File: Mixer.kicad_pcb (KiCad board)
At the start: 2 copper layers, 59.9 x 100 mm, 48 parts, among them J1 AudioJack2_Ground_Switch, J2 AudioJack2_Ground_Switch, J3 AudioJack2_Ground_Switch, J4 AudioJack2_Ground_Switch, J5 AudioJack2_Ground_Switch, J6 AudioJack2_Ground_Switch, J7 Conn_02x05_Odd_Even, U1 TL074

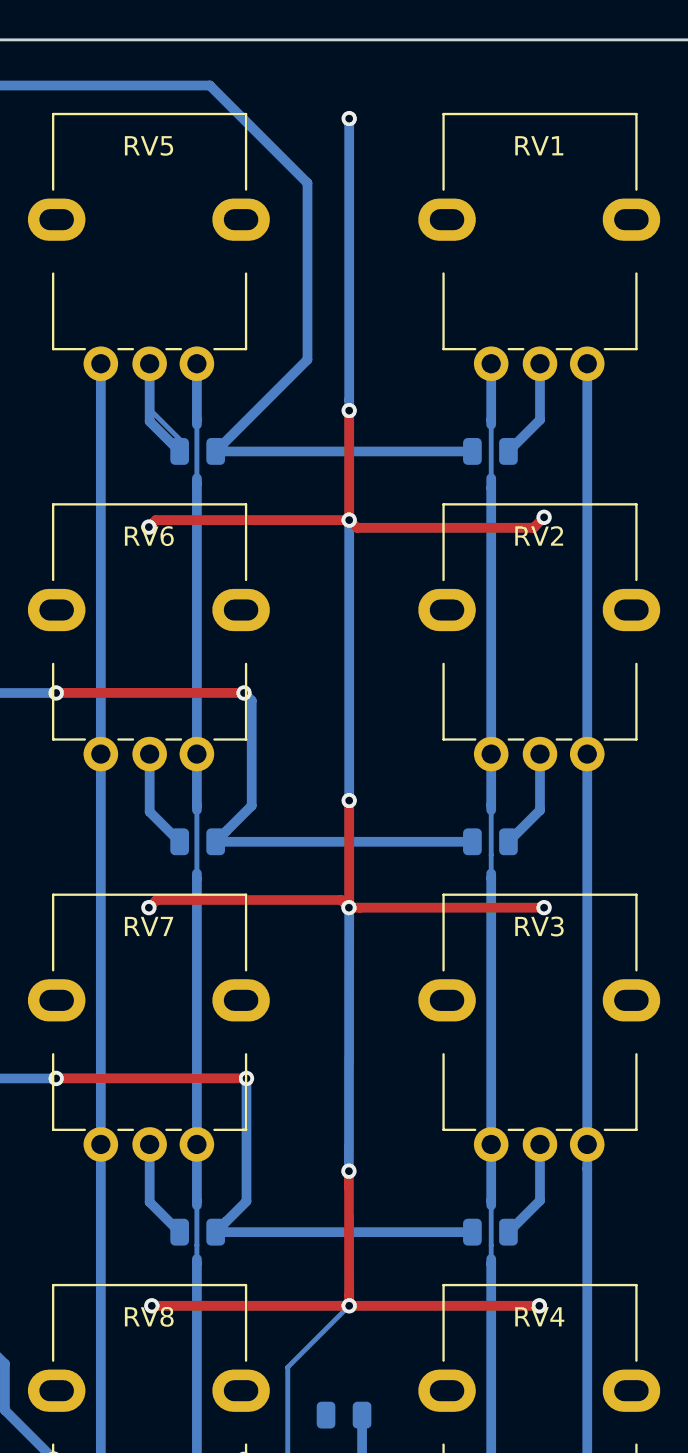
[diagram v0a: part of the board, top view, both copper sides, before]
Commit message: Updated silk-screen with voltages.
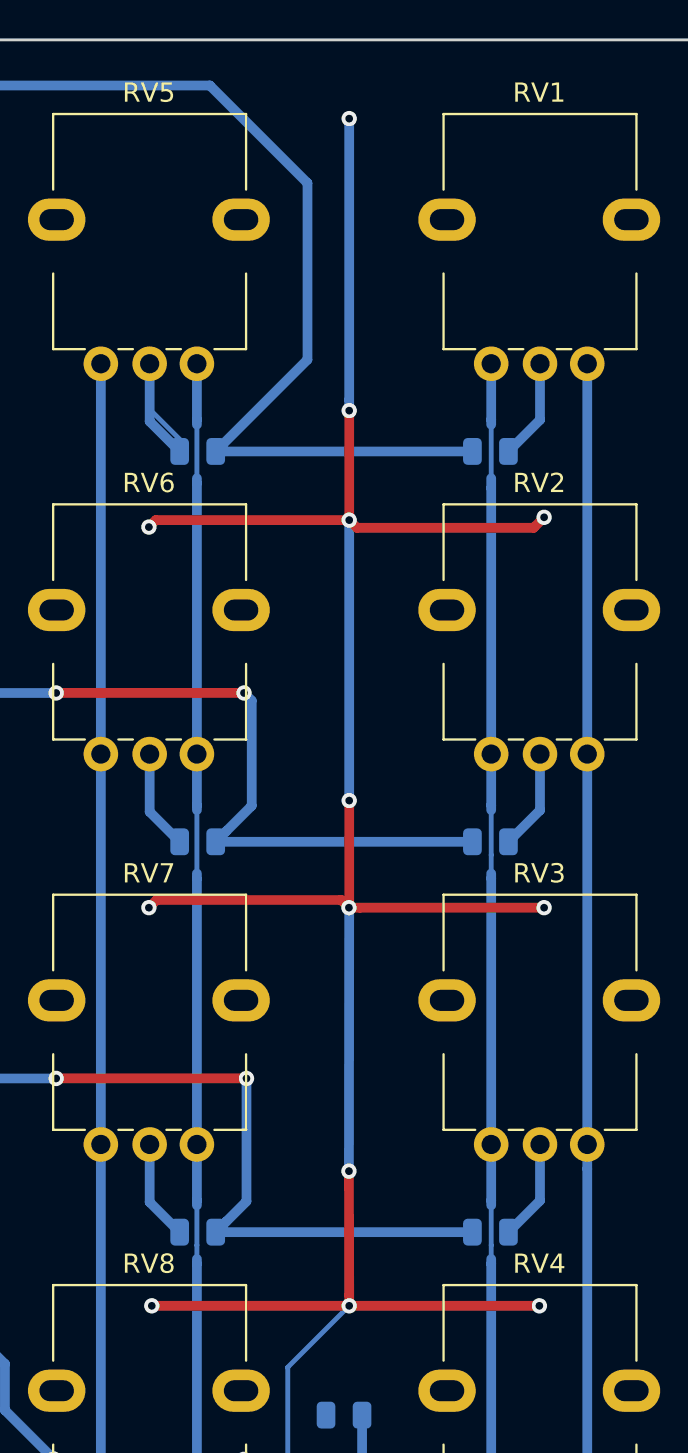
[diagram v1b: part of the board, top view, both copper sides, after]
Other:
- board text added: "+12"
- board text added: "-12"
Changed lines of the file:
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@@
   (general
     (thickness 1.6)
-    (drawings 61)
+    (drawings 64)
     (tracks 329)
     (zones 0)
@@
     (descr "Potentiometer, vertical, Alps RK09K Single, http://www.alps.com/prod/info/E/HTML/Potentiometer/RotaryPotentiometers/RK09K/RK09K_list.html")
     (tags "Potentiometer vertical Alps RK09K Single")
-    (fp_text reference RV8 (at 0 -3.81 180) (layer F.SilkS)
+    (fp_text reference RV8 (at 0 -6.604 180) (layer F.SilkS)
       (effects (font (size 1 1) (thickness 0.15)))
     )
@@
     (descr "Potentiometer, vertical, Alps RK09K Single, http://www.alps.com/prod/info/E/HTML/Potentiometer/RotaryPotentiometers/RK09K/RK09K_list.html")
     (tags "Potentiometer vertical Alps RK09K Single")
-    (fp_text reference RV7 (at 0 -3.81 180) (layer F.SilkS)
+    (fp_text reference RV7 (at 0 -6.604 180) (layer F.SilkS)
       (effects (font (size 1 1) (thickness 0.15)))
     )
@@
     (descr "Potentiometer, vertical, Alps RK09K Single, http://www.alps.com/prod/info/E/HTML/Potentiometer/RotaryPotentiometers/RK09K/RK09K_list.html")
     (tags "Potentiometer vertical Alps RK09K Single")
-    (fp_text reference RV6 (at 0 -3.81 180) (layer F.SilkS)
+    (fp_text reference RV6 (at 0 -6.604 180) (layer F.SilkS)
       (effects (font (size 1 1) (thickness 0.15)))
     )
@@
     (descr "Potentiometer, vertical, Alps RK09K Single, http://www.alps.com/prod/info/E/HTML/Potentiometer/RotaryPotentiometers/RK09K/RK09K_list.html")
     (tags "Potentiometer vertical Alps RK09K Single")
-    (fp_text reference RV5 (at 0 -3.81 180) (layer F.SilkS)
+    (fp_text reference RV5 (at 0 -6.604 180) (layer F.SilkS)
       (effects (font (size 1 1) (thickness 0.15)))
     )
@@
     (descr "Potentiometer, vertical, Alps RK09K Single, http://www.alps.com/prod/info/E/HTML/Potentiometer/RotaryPotentiometers/RK09K/RK09K_list.html")
     (tags "Potentiometer vertical Alps RK09K Single")
-    (fp_text reference RV4 (at 0 -3.81 180) (layer F.SilkS)
+    (fp_text reference RV4 (at 0 -6.604 180) (layer F.SilkS)
       (effects (font (size 1 1) (thickness 0.15)))
     )
@@
     (descr "Potentiometer, vertical, Alps RK09K Single, http://www.alps.com/prod/info/E/HTML/Potentiometer/RotaryPotentiometers/RK09K/RK09K_list.html")
     (tags "Potentiometer vertical Alps RK09K Single")
-    (fp_text reference RV3 (at 0 -3.81 180) (layer F.SilkS)
+    (fp_text reference RV3 (at 0 -6.604 180) (layer F.SilkS)
       (effects (font (size 1 1) (thickness 0.15)))
     )
@@
     (descr "Potentiometer, vertical, Alps RK09K Single, http://www.alps.com/prod/info/E/HTML/Potentiometer/RotaryPotentiometers/RK09K/RK09K_list.html")
     (tags "Potentiometer vertical Alps RK09K Single")
-    (fp_text reference RV1 (at 0 -3.81 180) (layer F.SilkS)
+    (fp_text reference RV1 (at 0 -6.604 180) (layer F.SilkS)
       (effects (font (size 1 1) (thickness 0.15)))
     )
@@
     (descr "Potentiometer, vertical, Alps RK09K Single, http://www.alps.com/prod/info/E/HTML/Potentiometer/RotaryPotentiometers/RK09K/RK09K_list.html")
     (tags "Potentiometer vertical Alps RK09K Single")
-    (fp_text reference RV2 (at 0 -3.81 180) (layer F.SilkS)
+    (fp_text reference RV2 (at 0 -6.604 180) (layer F.SilkS)
       (effects (font (size 1 1) (thickness 0.15)))
     )
@@
     )
   )
+  (gr_line (start 109.982 69.342) (end 104.902 69.342) (layer B.SilkS) (width 0.4))
+  (gr_text -12 (at 102.87 66.548) (layer B.SilkS)
+    (effects (font (size 1.2 1.2) (thickness 0.3)) (justify mirror))
+  )
+  (gr_text +12 (at 102.87 56.388) (layer B.SilkS)
+    (effects (font (size 1.2 1.2) (thickness 0.3)) (justify mirror))
+  )
   (gr_text "Rev B" (at 92.71 58.166 90) (layer B.SilkS)
